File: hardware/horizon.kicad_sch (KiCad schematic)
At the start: 58 parts, among them J1 Conn_01x02_Pin, J2 Conn_01x06_Pin, J3 USB_C_Receptacle_USB2.0_14P, J4 Conn_01x14_Pin, J5 Conn_01x02_Socket, J6 Conn_01x02_Pin, J7 SD_Card_Receptacle, Q1 NPN, SW1 SW_Push, SW2 SW_Push, U1 ESP32-S3, U2 NCP1529A, U3 W25Q128JVS, U4 BQ24074RGT, U5 DRV2605LDGS, U6 ESP-PSRAM64H, Y1 CDX-1293

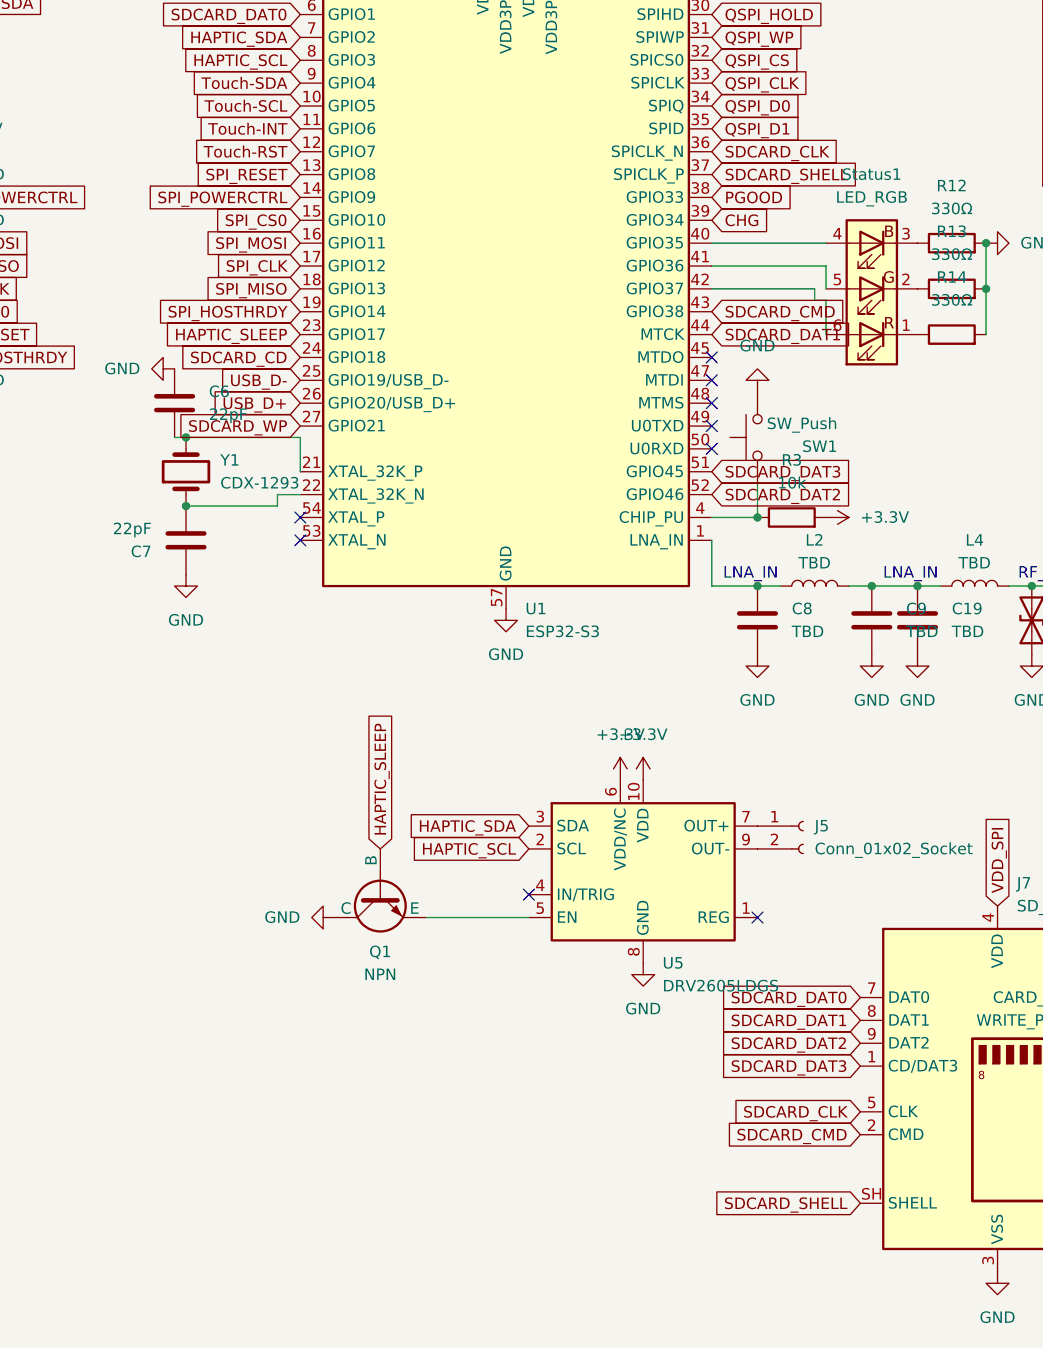
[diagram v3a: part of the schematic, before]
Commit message: Finished SD card wiring
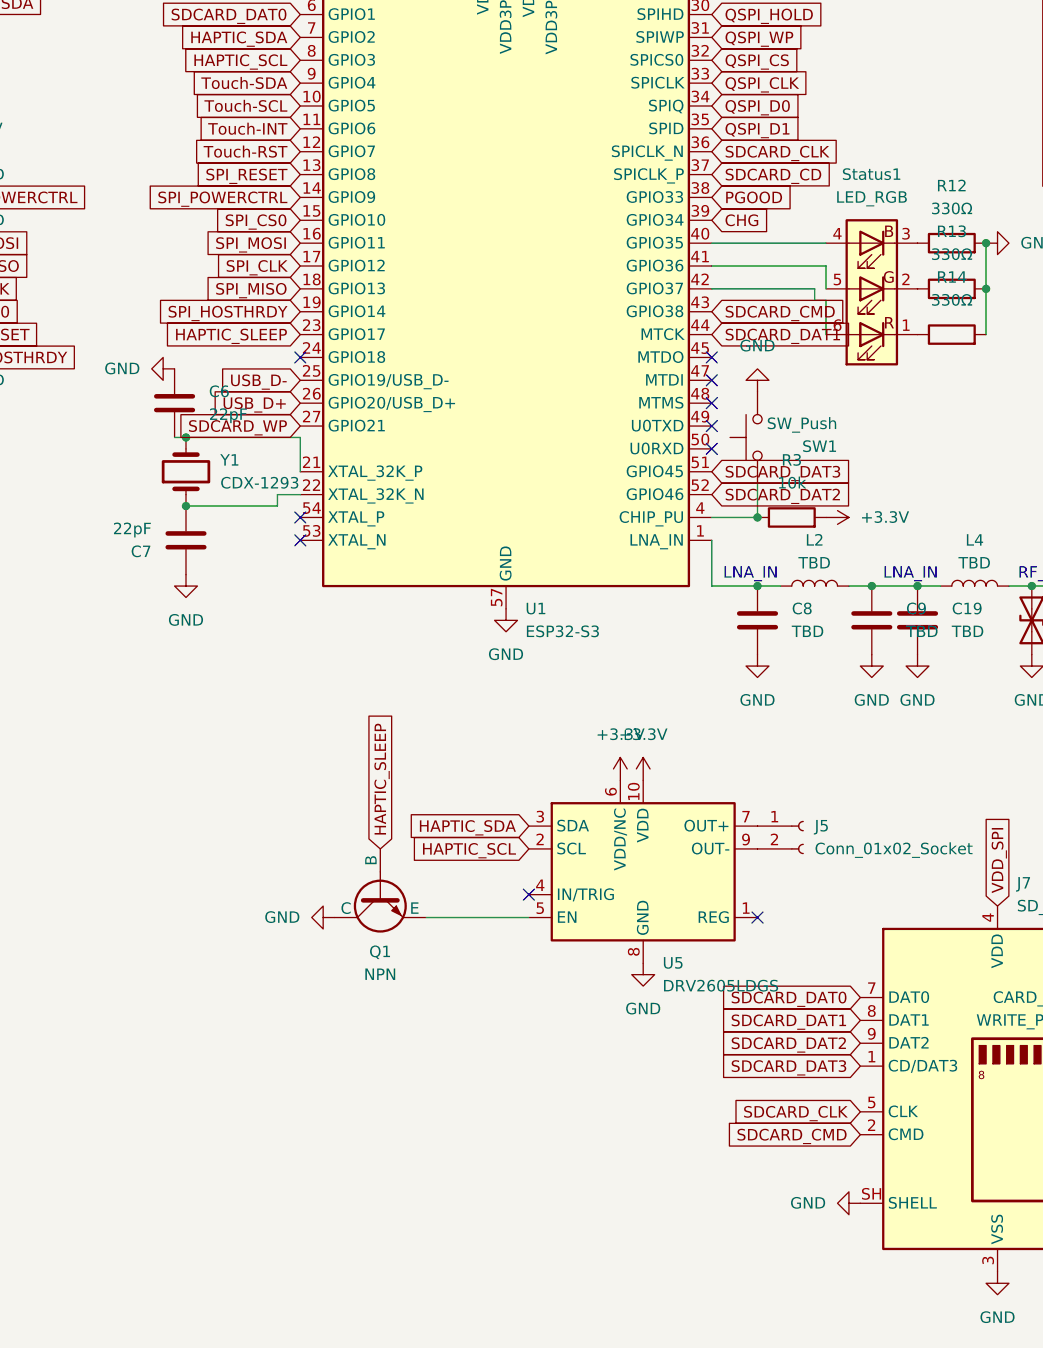
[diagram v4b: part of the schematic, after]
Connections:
- net GND: now also J7.SH (SHELL)
- net SDCARD_CD: now also U1.37 (SPICLK_P); no longer U1.24 (GPIO18)
- removed net SDCARD_SHELL: J7.SH (SHELL), U1.37 (SPICLK_P)
- no-connect marks 11 -> 12
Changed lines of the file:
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@@
 	)
 	(no_connect
+		(at 78.74 90.17)
+	)
+	(no_connect
 		(at 124.46 97.79)
 	)
@@
 		)
 	)
-	(global_label "SDCARD_SHELL"
-		(shape input)
-		(at 124.46 69.85 0)
-		(fields_autoplaced yes)
-		(effects
-			(font
-				(size 1.27 1.27)
-			)
-			(justify left)
-		)
-		(property "Intersheetrefs" "${INTERSHEET_REFS}"
-			(at 141.5361 69.85 0)
-			(hide yes)
-			(show_name no)
-			(do_not_autoplace no)
-			(effects
-				(font
-					(size 1.27 1.27)
-				)
-				(justify left)
-			)
-		)
-	)
 	(global_label "SPI_MISO"
 		(shape input)
@@
 		)
 	)
-	(global_label "SDCARD_CD"
-		(shape input)
-		(at 78.74 90.17 180)
-		(fields_autoplaced yes)
-		(effects
-			(font
-				(size 1.27 1.27)
-			)
-			(justify right)
-		)
-		(property "Intersheetrefs" "${INTERSHEET_REFS}"
-			(at 64.8691 90.17 0)
-			(hide yes)
-			(show_name no)
-			(do_not_autoplace no)
-			(effects
-				(font
-					(size 1.27 1.27)
-				)
-				(justify right)
-			)
-		)
-	)
 	(global_label "Touch-RST"
 		(shape input)
@@
 		)
 	)
-	(global_label "SDCARD_SHELL"
-		(shape input)
-		(at 140.97 184.15 180)
-		(fields_autoplaced yes)
-		(effects
-			(font
-				(size 1.27 1.27)
-			)
-			(justify right)
-		)
-		(property "Intersheetrefs" "${INTERSHEET_REFS}"
-			(at 123.8939 184.15 0)
-			(hide yes)
-			(show_name no)
-			(do_not_autoplace no)
-			(effects
-				(font
-					(size 1.27 1.27)
-				)
-				(justify right)
-			)
-		)
-	)
 	(global_label "USB_D+"
 		(shape input)
@@
 		)
 	)
+	(global_label "SDCARD_CD"
+		(shape input)
+		(at 124.46 69.85 0)
+		(fields_autoplaced yes)
+		(effects
+			(font
+				(size 1.27 1.27)
+			)
+			(justify left)
+		)
+		(property "Intersheetrefs" "${INTERSHEET_REFS}"
+			(at 138.3309 69.85 0)
+			(hide yes)
+			(show_name no)
+			(do_not_autoplace no)
+			(effects
+				(font
+					(size 1.27 1.27)
+				)
+				(justify left)
+			)
+		)
+	)
 	(global_label "Touch-INT"
 		(shape input)
@@
 					(unit 1)
 				)
+			)
+		)
+	)
+	(symbol
+		(lib_id "power:GND")
+		(at 140.97 184.15 270)
+		(unit 1)
+		(body_style 1)
+		(exclude_from_sim no)
+		(in_bom yes)
+		(on_board yes)
+		(in_pos_files yes)
+		(dnp no)
+		(fields_autoplaced yes)
+		(property "Reference" "#PWR065"
+			(at 134.62 184.15 0)
+			(hide yes)
+			(show_name no)
+			(do_not_autoplace no)
+			(effects
+				(font
+					(size 1.27 1.27)
+				)
+			)
+		)
+		(property "Value" "GND"
+			(at 137.16 184.1499 90)
+			(show_name no)
+			(do_not_autoplace no)
+			(effects
+				(font
+					(size 1.27 1.27)
+				)
+				(justify right)
+			)
+		)
+		(property "Footprint" ""
+			(at 140.97 184.15 0)
+			(hide yes)
+			(show_name no)
+			(do_not_autoplace no)
+			(effects
+				(font
+					(size 1.27 1.27)
+				)
+			)
+		)
+		(property "Datasheet" ""
+			(at 140.97 184.15 0)
+			(hide yes)
+			(show_name no)
+			(do_not_autoplace no)
+			(effects
+				(font
+					(size 1.27 1.27)
+				)
+			)
+		)
+		(property "Description" "Power symbol creates a global label with name \"GND\" , ground"
+			(at 140.97 184.15 0)
+			(hide yes)
+			(show_name no)
+			(do_not_autoplace no)
+			(effects
+				(font
+					(size 1.27 1.27)
+				)
+			)
+		)
+		(pin "1"
+		)
+		(instances
+			(project "horizon"
+				(path "/b7fe370f-670d-489a-828f-5e84b63a70c0"
+					(reference "#PWR065")
+					(unit 1)
+				)

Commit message: Fixed connectors
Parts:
- J2: footprint Connector_PinHeader_2.54mm:PinHeader_1x06_P2.54mm_Horizontal -> Connector_FFC-FPC:Hirose_FH12-6S-0.5SH_1x06-1MP_P0.50mm_Horizontal
- J4: footprint Connector_PinHeader_2.54mm:PinHeader_1x14_P2.54mm_Horizontal -> Connector_FFC-FPC:Hirose_FH12-14S-0.5SH_1x14-1MP_P0.50mm_Horizontal
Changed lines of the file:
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@@
 	)
 	(no_connect
-		(at 78.74 90.17)
-	)
-	(no_connect
 		(at 124.46 97.79)
 	)
@@
 	)
 	(no_connect
+		(at 78.74 90.17)
+	)
+	(no_connect
 		(at 124.46 92.71)
 	)
@@
 		)
 	)
+	(global_label "SDCARD_CD"
+		(shape input)
+		(at 124.46 69.85 0)
+		(fields_autoplaced yes)
+		(effects
+			(font
+				(size 1.27 1.27)
+			)
+			(justify left)
+		)
+		(property "Intersheetrefs" "${INTERSHEET_REFS}"
+			(at 138.3309 69.85 0)
+			(hide yes)
+			(show_name no)
+			(do_not_autoplace no)
+			(effects
+				(font
+					(size 1.27 1.27)
+				)
+				(justify left)
+			)
+		)
+	)
 	(global_label "QSPI_WP"
 		(shape input)
@@
 		)
 	)
-	(global_label "SDCARD_CD"
-		(shape input)
-		(at 124.46 69.85 0)
-		(fields_autoplaced yes)
-		(effects
-			(font
-				(size 1.27 1.27)
-			)
-			(justify left)
-		)
-		(property "Intersheetrefs" "${INTERSHEET_REFS}"
-			(at 138.3309 69.85 0)
-			(hide yes)
-			(show_name no)
-			(do_not_autoplace no)
-			(effects
-				(font
-					(size 1.27 1.27)
-				)
-				(justify left)
-			)
-		)
-	)
 	(global_label "Touch-INT"
 		(shape input)
@@
 			)
 		)
-		(property "Footprint" "Connector_PinHeader_2.54mm:PinHeader_1x06_P2.54mm_Horizontal"
+		(property "Footprint" "Connector_FFC-FPC:Hirose_FH12-6S-0.5SH_1x06-1MP_P0.50mm_Horizontal"
 			(at 33.02 43.18 0)
 			(hide yes)
@@
 	)
 	(symbol
-		(lib_id "power:GND")
-		(at 140.97 184.15 270)
-		(unit 1)
-		(body_style 1)
-		(exclude_from_sim no)
-		(in_bom yes)
-		(on_board yes)
-		(in_pos_files yes)
-		(dnp no)
-		(fields_autoplaced yes)
-		(property "Reference" "#PWR065"
-			(at 134.62 184.15 0)
-			(hide yes)
-			(show_name no)
-			(do_not_autoplace no)
-			(effects
-				(font
-					(size 1.27 1.27)
-				)
-			)
-		)
-		(property "Value" "GND"
-			(at 137.16 184.1499 90)
-			(show_name no)
-			(do_not_autoplace no)
-			(effects
-				(font
-					(size 1.27 1.27)
-				)
-				(justify right)
-			)
-		)
-		(property "Footprint" ""
-			(at 140.97 184.15 0)
-			(hide yes)
-			(show_name no)
-			(do_not_autoplace no)
-			(effects
-				(font
-					(size 1.27 1.27)
-				)
-			)
-		)
-		(property "Datasheet" ""
-			(at 140.97 184.15 0)
-			(hide yes)
-			(show_name no)
-			(do_not_autoplace no)
-			(effects
-				(font
-					(size 1.27 1.27)
-				)
-			)
-		)
-		(property "Description" "Power symbol creates a global label with name \"GND\" , ground"
-			(at 140.97 184.15 0)
-			(hide yes)
-			(show_name no)
-			(do_not_autoplace no)
-			(effects
-				(font
-					(size 1.27 1.27)
-				)
-			)
-		)
-		(pin "1"
-		)
-		(instances
-			(project "horizon"
-				(path "/b7fe370f-670d-489a-828f-5e84b63a70c0"
-					(reference "#PWR065")
-					(unit 1)
-				)
-			)
-		)
-	)
-	(symbol
 		(lib_id "Device:C")
 		(at 123.19 19.05 180)
@@
 			)
 		)
-		(property "Footprint" "Connector_PinHeader_2.54mm:PinHeader_1x14_P2.54mm_Horizontal"
+		(property "Footprint" "Connector_FFC-FPC:Hirose_FH12-14S-0.5SH_1x14-1MP_P0.50mm_Horizontal"
 			(at 33.02 74.93 0)
 			(hide yes)
@@
 					(unit 1)
 				)
+			)
+		)
+	)
+	(symbol
+		(lib_id "power:GND")
+		(at 140.97 184.15 270)
+		(unit 1)
+		(body_style 1)
+		(exclude_from_sim no)
+		(in_bom yes)
+		(on_board yes)
+		(in_pos_files yes)
+		(dnp no)
+		(fields_autoplaced yes)
+		(property "Reference" "#PWR065"
+			(at 134.62 184.15 0)
+			(hide yes)
+			(show_name no)
+			(do_not_autoplace no)
+			(effects
+				(font
+					(size 1.27 1.27)
+				)
+			)
+		)
+		(property "Value" "GND"
+			(at 137.16 184.1499 90)
+			(show_name no)
+			(do_not_autoplace no)
+			(effects
+				(font
+					(size 1.27 1.27)
+				)
+				(justify right)
+			)
+		)
+		(property "Footprint" ""
+			(at 140.97 184.15 0)
+			(hide yes)
+			(show_name no)
+			(do_not_autoplace no)
+			(effects
+				(font
+					(size 1.27 1.27)
+				)
+			)
+		)
+		(property "Datasheet" ""
+			(at 140.97 184.15 0)
+			(hide yes)
+			(show_name no)
+			(do_not_autoplace no)
+			(effects
+				(font
+					(size 1.27 1.27)
+				)
+			)
+		)
+		(property "Description" "Power symbol creates a global label with name \"GND\" , ground"
+			(at 140.97 184.15 0)
+			(hide yes)
+			(show_name no)
+			(do_not_autoplace no)
+			(effects
+				(font
+					(size 1.27 1.27)
+				)
+			)
+		)
+		(pin "1"
+		)
+		(instances
+			(project "horizon"
+				(path "/b7fe370f-670d-489a-828f-5e84b63a70c0"
+					(reference "#PWR065")
+					(unit 1)
+				)
